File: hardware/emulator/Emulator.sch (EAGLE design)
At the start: 28 parts, among them U1 PDM1-S5-D12-S, U2 LM6132BIN, U3 OPA2277PA, U4 L7908CV, U5 L7808ABV, U6 TEENSY_3.6_DIL, U7 ZVP2106ASTZ

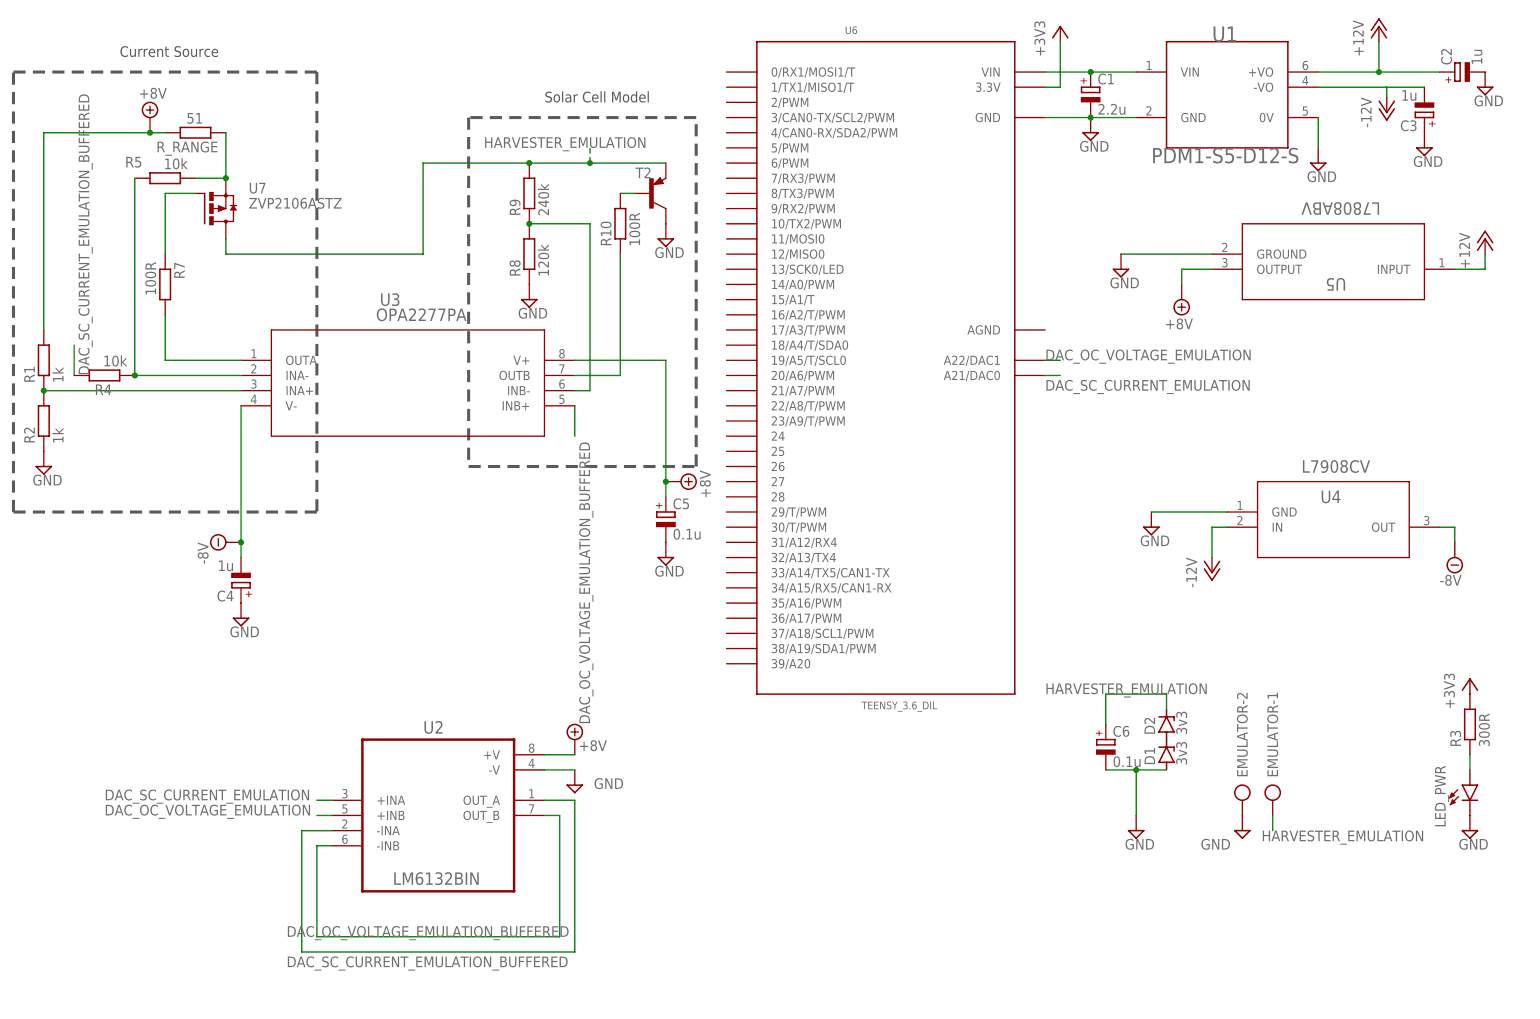
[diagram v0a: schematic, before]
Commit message: Update emulator hardware
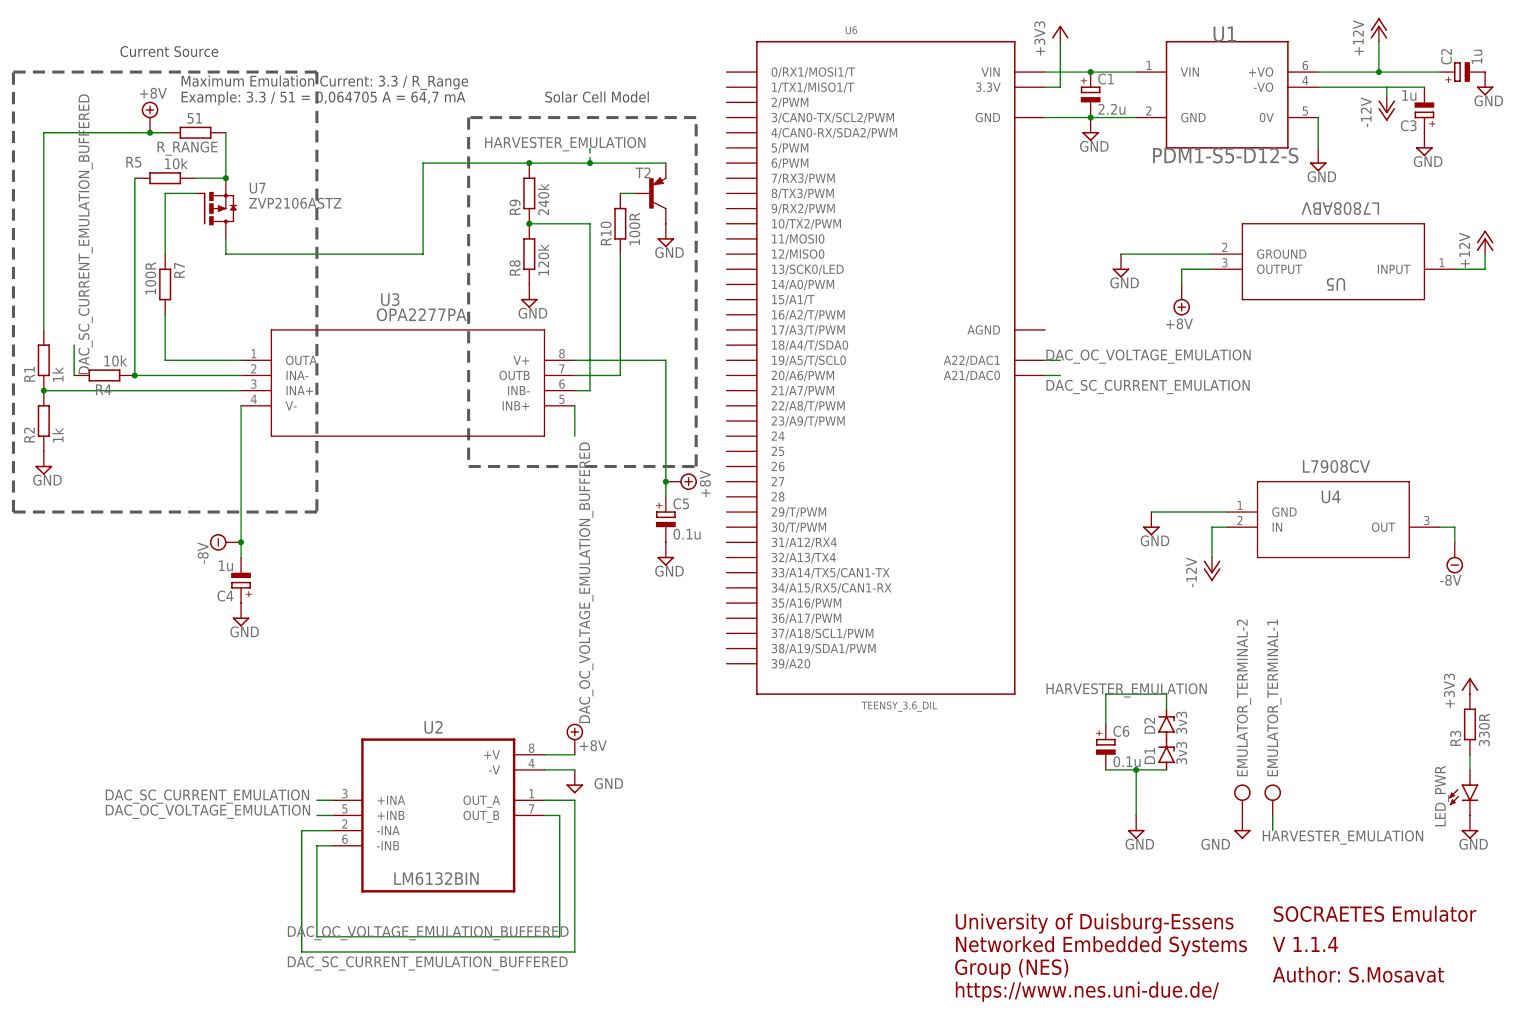
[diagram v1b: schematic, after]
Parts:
- R3: value 300R -> 330R
- renumbered EMULATOR to EMULATOR_TERMINAL
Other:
- note added: "Author: S.Mosavat"
- note added: "Maximum Emulation Current: 3.3 / R_Range Example: 3.3 / 51 = 0,064705 A = 64,7 mA"
- note added: "SOCRAETES Emulator"
- note added: "University of Duisburg-Essens Networked Embedded Systems Group (NES) https://www.nes.uni-due.de/"
- note added: "V 1.1.4"
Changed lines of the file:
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@@
 <parts>
 <part name="U1" library="PDM1-S5-D12-S" deviceset="PDM1-S5-D12-S" device=""/>
-<part name="EMULATOR" library="con-ptr500" library_urn="urn:adsk.eagle:library:181" deviceset="AK300/2" device="" package3d_urn="urn:adsk.eagle:package:9881/1"/>
+<part name="EMULATOR_TERMINAL" library="con-ptr500" library_urn="urn:adsk.eagle:library:181" deviceset="AK300/2" device="" package3d_urn="urn:adsk.eagle:package:9881/1"/>
 <part name="D1" library="diode" library_urn="urn:adsk.eagle:library:210" deviceset="ZENER-DIODE" device="ZD-7.5" package3d_urn="urn:adsk.eagle:package:43411/1" value="3v3"/>
 <part name="U2" library="LM6132BIN" deviceset="LM6132BIN" device=""/>
@@
 <part name="+3V2" library="supply1" library_urn="urn:adsk.eagle:library:371" deviceset="+3V3" device=""/>
 <part name="SUPPLY21" library="supply2" library_urn="urn:adsk.eagle:library:372" deviceset="GND" device=""/>
-<part name="R3" library="rcl" library_urn="urn:adsk.eagle:library:334" deviceset="R-EU_" device="0207/10" package3d_urn="urn:adsk.eagle:package:23491/2" value="300R"/>
+<part name="R3" library="rcl" library_urn="urn:adsk.eagle:library:334" deviceset="R-EU_" device="0207/10" package3d_urn="urn:adsk.eagle:package:23491/2" value="330R"/>
 <part name="LED_PWR" library="led" library_urn="urn:adsk.eagle:library:259" deviceset="LED" device="5MM" package3d_urn="urn:adsk.eagle:package:15799/2"/>
 <part name="U3" library="OPA2277PA" deviceset="OPA2277PA" device=""/>
@@
 <wire x1="119.38" y1="154.94" x2="81.28" y2="154.94" width="0.508" layer="97" style="longdash"/>
 <text x="93.98" y="157.48" size="1.778" layer="97">Solar Cell Model</text>
+<text x="33.02" y="157.48" size="1.778" layer="97">Maximum Emulation Current: 3.3 / R_Range
+Example: 3.3 / 51 = 0,064705 A = 64,7 mA</text>
+<text x="215.9" y="20.32" size="2.54" layer="94">SOCRAETES Emulator</text>
+<text x="215.9" y="15.24" size="2.54" layer="94">V 1.1.4</text>
+<text x="215.9" y="10.16" size="2.54" layer="94">Author: S.Mosavat</text>
+<text x="162.56" y="7.62" size="2.54" layer="94">University of Duisburg-Essens
+Networked Embedded Systems
+Group (NES)
+https://www.nes.uni-due.de/</text>
 </plain>
 <instances>
@@
 <attribute name="VALUE" x="195.5677" y="149.8477" size="2.54308125" layer="96" align="top-left"/>
 </instance>
-<instance part="EMULATOR" gate="-1" x="215.9" y="43.18" smashed="yes" rot="R270">
+<instance part="EMULATOR_TERMINAL" gate="-1" x="215.9" y="43.18" smashed="yes" rot="R270">
 <attribute name="NAME" x="216.789" y="44.45" size="1.778" layer="95" rot="R90"/>
 </instance>
-<instance part="EMULATOR" gate="-2" x="210.82" y="43.18" smashed="yes" rot="R270">
+<instance part="EMULATOR_TERMINAL" gate="-2" x="210.82" y="43.18" smashed="yes" rot="R270">
 <attribute name="NAME" x="211.709" y="44.45" size="1.778" layer="95" rot="R90"/>
 <attribute name="VALUE" x="207.137" y="46.99" size="1.778" layer="96" rot="R270"/>
@@
 </instance>
 <instance part="FRAME1" gate="G$1" x="0" y="0" smashed="yes">
-<attribute name="DRAWING_NAME" x="217.17" y="15.24" size="2.54" layer="94"/>
-<attribute name="LAST_DATE_TIME" x="217.17" y="10.16" size="2.286" layer="94"/>
 <attribute name="SHEET" x="230.505" y="5.08" size="2.54" layer="94"/>
 </instance>
@@
 </segment>
 <segment>
-<pinref part="EMULATOR" gate="-2" pin="KL"/>
+<pinref part="EMULATOR_TERMINAL" gate="-2" pin="KL"/>
 <pinref part="SUPPLY15" gate="GND" pin="GND"/>
 </segment>
@@
 <net name="HARVESTER_EMULATION" class="0">
 <segment>
-<pinref part="EMULATOR" gate="-1" pin="KL"/>
+<pinref part="EMULATOR_TERMINAL" gate="-1" pin="KL"/>
 <wire x1="215.9" y1="38.1" x2="215.9" y2="35.56" width="0.1524" layer="91"/>
 <label x="241.3" y="35.56" size="1.778" layer="95" rot="R180"/>
@@
 </drawing>
 <compatibility>
+<note version="6.3" minversion="6.2.2" severity="warning">
+Since Version 6.2.2 text objects can contain more than one line,
+which will not be processed correctly with this version.
+</note>
 <note version="8.2" severity="warning">
 Since Version 8.2, EAGLE supports online libraries. The ids

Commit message: Add a capacitor to the solar cell model op amp for stability of the op amp's output
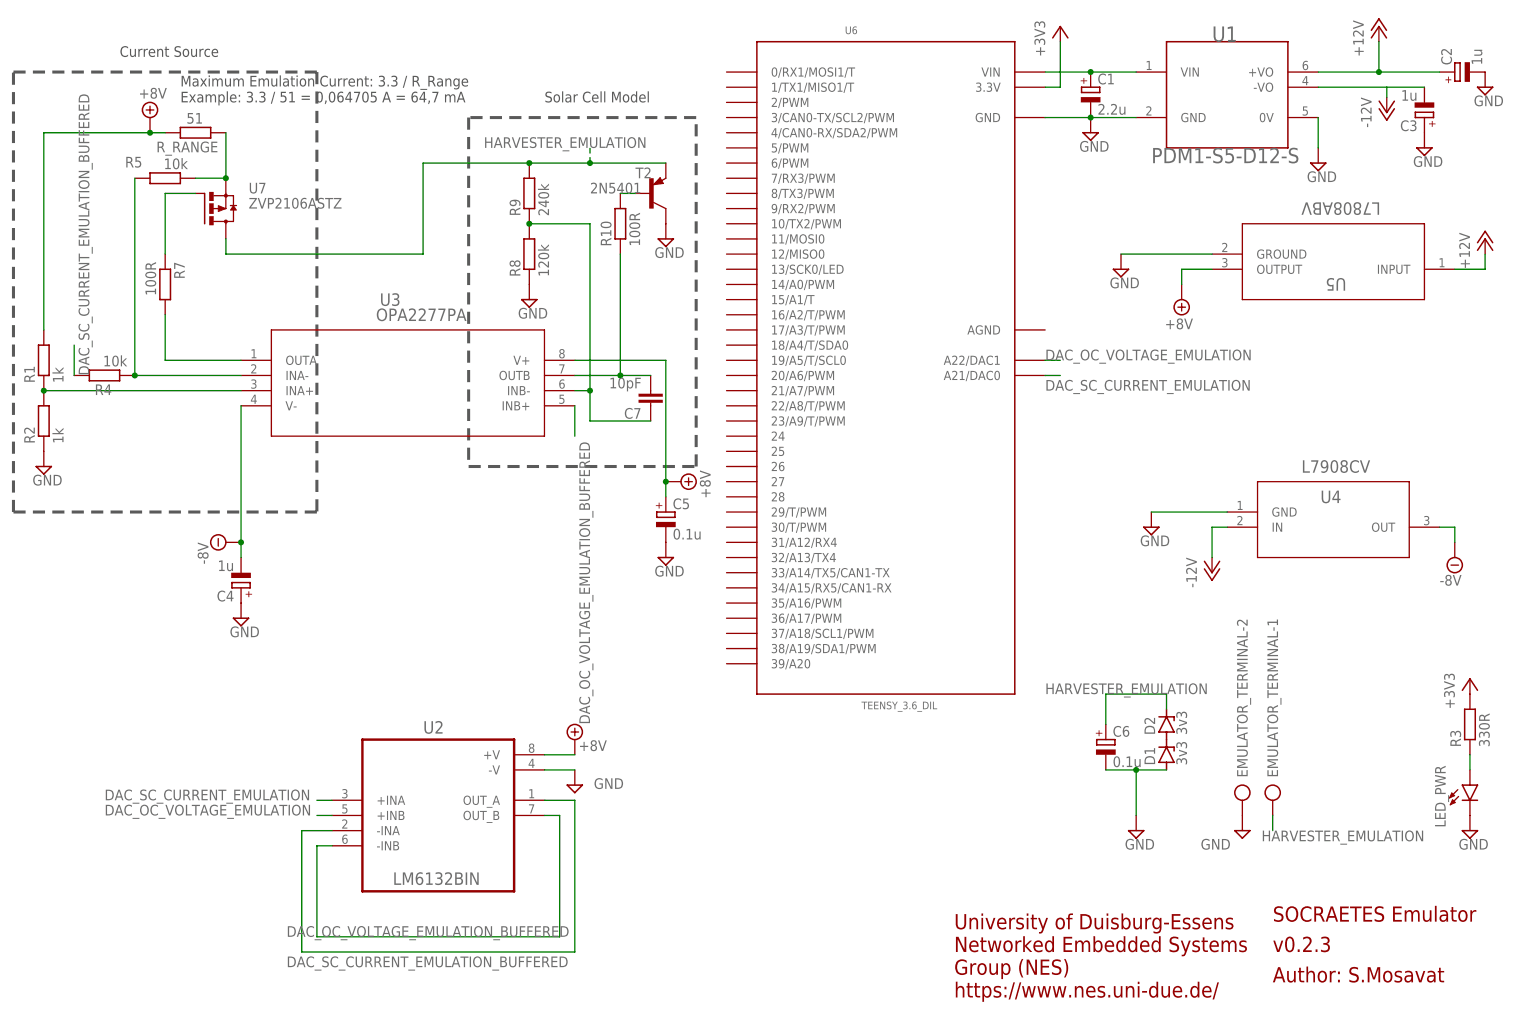
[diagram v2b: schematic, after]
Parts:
- added C7: 10pF, rcl:C-EU050-025X075
- T2: value (none) -> 2N5401
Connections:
- net N$11: now also C7.1
- net N$13: now also C7.2
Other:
- note added: "v0.2.3"
- note removed: "V 1.1.4"

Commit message: Add minor changes to the schematics
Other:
- note added: "I_OUT = DAC_SC / R_RANGE"
- note added: "University of Duisburg-Essen Networked Embedded Systems Group (NES) https://www.nes.uni-due.de/"
- note removed: "University of Duisburg-Essens Networked Embedded Systems Group (NES) https://www.nes.uni-due.de/"
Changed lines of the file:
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@@
 <grid distance="0.1" unitdist="inch" unit="inch" style="lines" multiple="1" display="no" altdistance="0.01" altunitdist="inch" altunit="inch"/>
 <layers>
-<layer number="1" name="Top" color="4" fill="1" visible="yes" active="no"/>
-<layer number="2" name="Route2" color="16" fill="1" visible="yes" active="no"/>
-<layer number="3" name="Route3" color="17" fill="1" visible="yes" active="no"/>
-<layer number="4" name="Route4" color="18" fill="1" visible="yes" active="no"/>
-<layer number="5" name="Route5" color="19" fill="1" visible="yes" active="no"/>
-<layer number="6" name="Route6" color="25" fill="1" visible="yes" active="no"/>
-<layer number="7" name="Route7" color="26" fill="1" visible="yes" active="no"/>
-<layer number="8" name="Route8" color="27" fill="1" visible="yes" active="no"/>
-<layer number="9" name="Route9" color="28" fill="1" visible="yes" active="no"/>
-<layer number="10" name="Route10" color="29" fill="1" visible="yes" active="no"/>
-<layer number="11" name="Route11" color="30" fill="1" visible="yes" active="no"/>
-<layer number="12" name="Route12" color="20" fill="1" visible="yes" active="no"/>
-<layer number="13" name="Route13" color="21" fill="1" visible="yes" active="no"/>
-<layer number="14" name="Route14" color="22" fill="1" visible="yes" active="no"/>
-<layer number="15" name="Route15" color="23" fill="1" visible="yes" active="no"/>
-<layer number="16" name="Bottom" color="1" fill="1" visible="yes" active="no"/>
-<layer number="17" name="Pads" color="2" fill="1" visible="yes" active="no"/>
-<layer number="18" name="Vias" color="2" fill="1" visible="yes" active="no"/>
-<layer number="19" name="Unrouted" color="6" fill="1" visible="yes" active="no"/>
-<layer number="20" name="Dimension" color="24" fill="1" visible="yes" active="no"/>
-<layer number="21" name="tPlace" color="7" fill="1" visible="yes" active="no"/>
-<layer number="22" name="bPlace" color="7" fill="1" visible="yes" active="no"/>
-<layer number="23" name="tOrigins" color="15" fill="1" visible="yes" active="no"/>
-<layer number="24" name="bOrigins" color="15" fill="1" visible="yes" active="no"/>
-<layer number="25" name="tNames" color="7" fill="1" visible="yes" active="no"/>
-<layer number="26" name="bNames" color="7" fill="1" visible="yes" active="no"/>
-<layer number="27" name="tValues" color="7" fill="1" visible="yes" active="no"/>
-<layer number="28" name="bValues" color="7" fill="1" visible="yes" active="no"/>
+<layer number="1" name="Top" color="4" fill="1" visible="no" active="no"/>
+<layer number="2" name="Route2" color="16" fill="1" visible="no" active="no"/>
+<layer number="3" name="Route3" color="17" fill="1" visible="no" active="no"/>
+<layer number="4" name="Route4" color="18" fill="1" visible="no" active="no"/>
+<layer number="5" name="Route5" color="19" fill="1" visible="no" active="no"/>
+<layer number="6" name="Route6" color="25" fill="1" visible="no" active="no"/>
+<layer number="7" name="Route7" color="26" fill="1" visible="no" active="no"/>
+<layer number="8" name="Route8" color="27" fill="1" visible="no" active="no"/>
+<layer number="9" name="Route9" color="28" fill="1" visible="no" active="no"/>
+<layer number="10" name="Route10" color="29" fill="1" visible="no" active="no"/>
+<layer number="11" name="Route11" color="30" fill="1" visible="no" active="no"/>
+<layer number="12" name="Route12" color="20" fill="1" visible="no" active="no"/>
+<layer number="13" name="Route13" color="21" fill="1" visible="no" active="no"/>
+<layer number="14" name="Route14" color="22" fill="1" visible="no" active="no"/>
+<layer number="15" name="Route15" color="23" fill="1" visible="no" active="no"/>
+<layer number="16" name="Bottom" color="1" fill="1" visible="no" active="no"/>
+<layer number="17" name="Pads" color="2" fill="1" visible="no" active="no"/>
+<layer number="18" name="Vias" color="2" fill="1" visible="no" active="no"/>
+<layer number="19" name="Unrouted" color="6" fill="1" visible="no" active="no"/>
+<layer number="20" name="Dimension" color="24" fill="1" visible="no" active="no"/>
+<layer number="21" name="tPlace" color="7" fill="1" visible="no" active="no"/>
+<layer number="22" name="bPlace" color="7" fill="1" visible="no" active="no"/>
+<layer number="23" name="tOrigins" color="15" fill="1" visible="no" active="no"/>
+<layer number="24" name="bOrigins" color="15" fill="1" visible="no" active="no"/>
+<layer number="25" name="tNames" color="7" fill="1" visible="no" active="no"/>
+<layer number="26" name="bNames" color="7" fill="1" visible="no" active="no"/>
+<layer number="27" name="tValues" color="7" fill="1" visible="no" active="no"/>
+<layer number="28" name="bValues" color="7" fill="1" visible="no" active="no"/>
 <layer number="29" name="tStop" color="7" fill="3" visible="no" active="no"/>
 <layer number="30" name="bStop" color="7" fill="6" visible="no" active="no"/>
@@
 <layer number="35" name="tGlue" color="7" fill="4" visible="no" active="no"/>
 <layer number="36" name="bGlue" color="7" fill="5" visible="no" active="no"/>
-<layer number="37" name="tTest" color="7" fill="1" visible="yes" active="no"/>
-<layer number="38" name="bTest" color="7" fill="1" visible="yes" active="no"/>
+<layer number="37" name="tTest" color="7" fill="1" visible="no" active="no"/>
+<layer number="38" name="bTest" color="7" fill="1" visible="no" active="no"/>
 <layer number="39" name="tKeepout" color="4" fill="11" visible="no" active="no"/>
 <layer number="40" name="bKeepout" color="1" fill="11" visible="no" active="no"/>
@@
 <layer number="44" name="Drills" color="7" fill="1" visible="no" active="no"/>
 <layer number="45" name="Holes" color="7" fill="1" visible="no" active="no"/>
-<layer number="46" name="Milling" color="3" fill="1" visible="yes" active="no"/>
-<layer number="47" name="Measures" color="7" fill="1" visible="yes" active="no"/>
-<layer number="48" name="Document" color="7" fill="1" visible="yes" active="no"/>
-<layer number="49" name="Reference" color="7" fill="1" visible="yes" active="no"/>
-<layer number="51" name="tDocu" color="7" fill="1" visible="yes" active="no"/>
-<layer number="52" name="bDocu" color="7" fill="1" visible="yes" active="no"/>
+<layer number="46" name="Milling" color="3" fill="1" visible="no" active="no"/>
+<layer number="47" name="Measures" color="7" fill="1" visible="no" active="no"/>
+<layer number="48" name="Document" color="7" fill="1" visible="no" active="no"/>
+<layer number="49" name="Reference" color="7" fill="1" visible="no" active="no"/>
+<layer number="51" name="tDocu" color="7" fill="1" visible="no" active="no"/>
+<layer number="52" name="bDocu" color="7" fill="1" visible="no" active="no"/>
 <layer number="88" name="SimResults" color="9" fill="1" visible="yes" active="yes"/>
 <layer number="89" name="SimProbes" color="9" fill="1" visible="yes" active="yes"/>
@@
 <text x="215.9" y="15.24" size="2.54" layer="94">v0.2.3</text>
 <text x="215.9" y="10.16" size="2.54" layer="94">Author: S.Mosavat</text>
-<text x="162.56" y="7.62" size="2.54" layer="94">University of Duisburg-Essens
+<text x="162.56" y="7.62" size="2.54" layer="94">University of Duisburg-Essen
 Networked Embedded Systems
 Group (NES)
 https://www.nes.uni-due.de/</text>
+<text x="40.64" y="129.54" size="1.778" layer="97">I_OUT = DAC_SC / R_RANGE</text>
 </plain>
 <instances>
